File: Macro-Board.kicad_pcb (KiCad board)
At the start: 2 copper layers, 215.9 x 139.7 mm, 62 parts, among them J1 esp32row1, J2 esp32row1, K1 KEYSW, K10 KEYSW, K11 KEYSW, K12 KEYSW, K13 KEYSW, K14 KEYSW, K15 KEYSW, K16 KEYSW, K17 KEYSW, K18 KEYSW, K19 KEYSW, K2 KEYSW, K20 KEYSW, K21 KEYSW, K22 KEYSW, K23 KEYSW, K24 KEYSW, K25 KEYSW, K27 KEYSW, K28 KEYSW, K29 KEYSW, K3 KEYSW, K30 KEYSW, K4 KEYSW, K5 KEYSW, K6 KEYSW, K7 KEYSW, K8 KEYSW, K9 KEYSW, SW26 RotaryEncoder_Alps_EC11E-Swit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

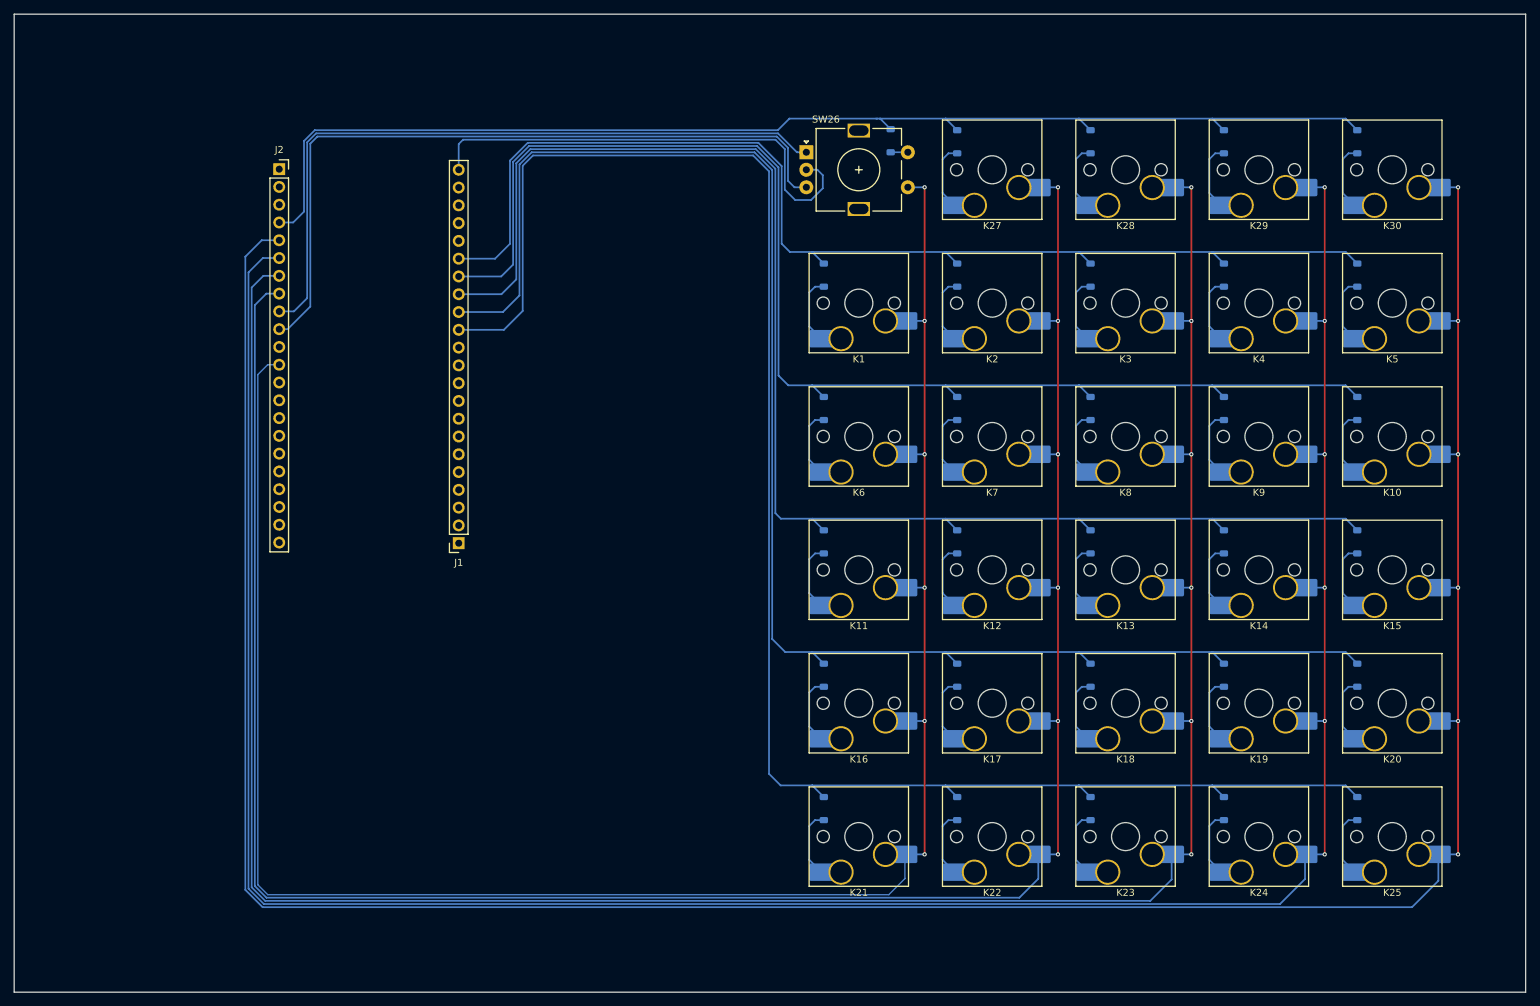
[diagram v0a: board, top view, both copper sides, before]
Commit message: Added PCB Edge + Updated Encoder Library
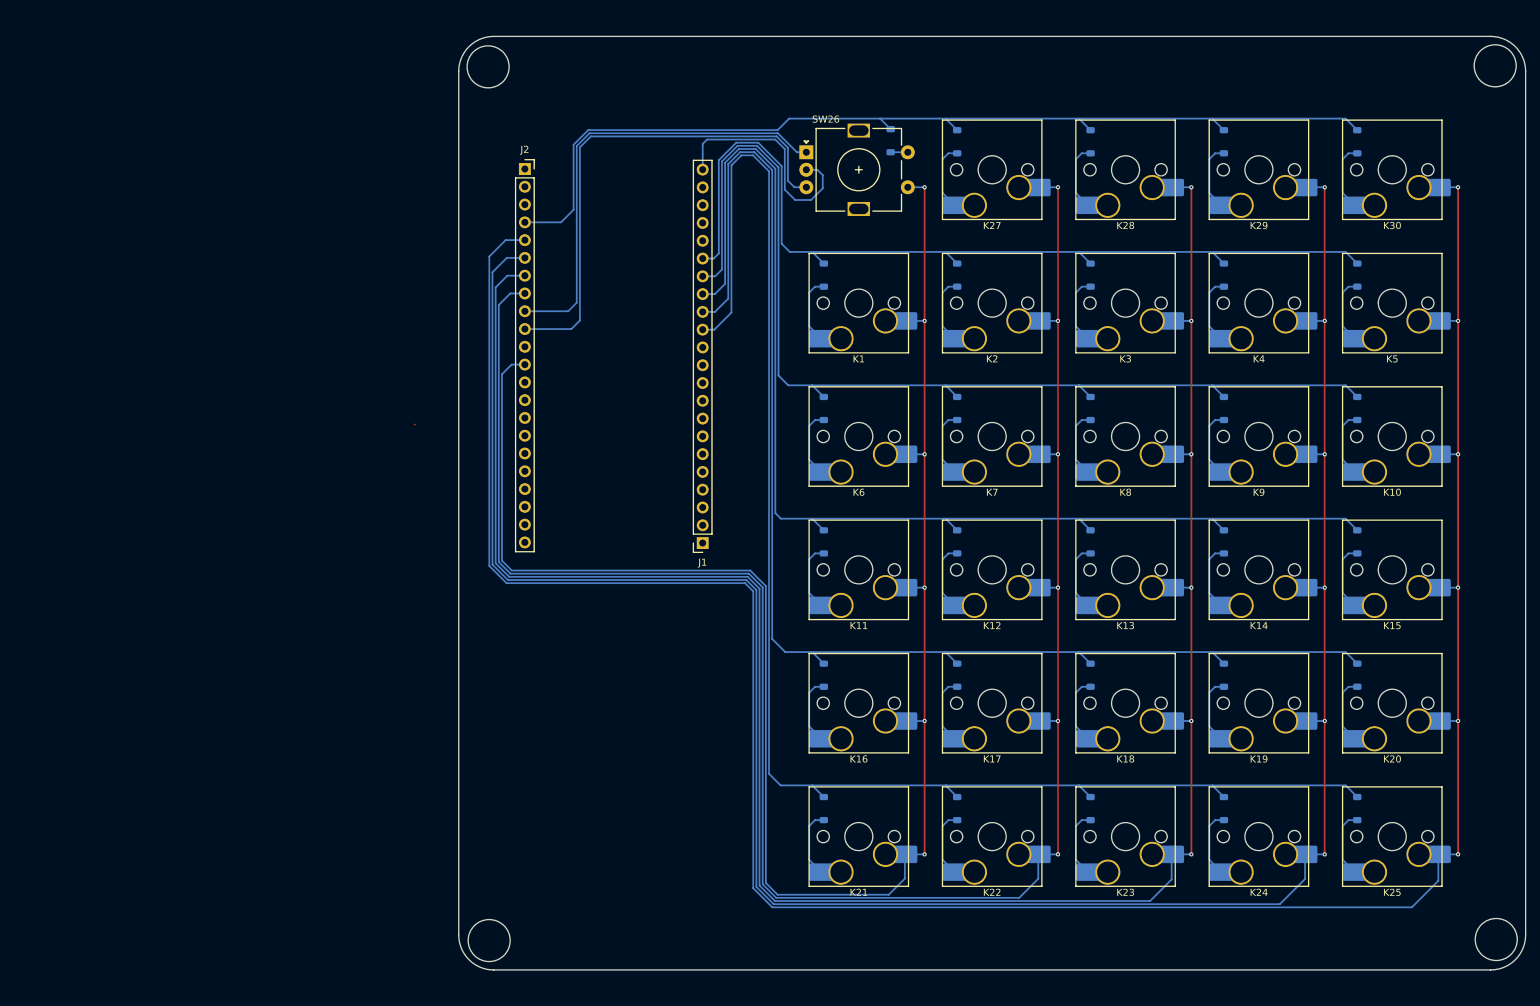
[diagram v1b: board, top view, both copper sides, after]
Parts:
- moved J2 35.1 mm to (-47.7, -19.2)
- moved J1 34.9 mm to (-22.3, 34.3)
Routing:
- net /GPIO08: track 285.7 -> 248.6 mm
- net /GPIO05: track 384.8 -> 347.7 mm
- net /GPIO06: track 361.9 -> 324.8 mm
- net /GPIO07: track 339.1 -> 302.0 mm
- net /GPIO15: track 316.1 -> 279.0 mm
- net /GPIO04: track 175.9 -> 140.6 mm
- net /GND4: track 68.1 -> 33.3 mm
- net /EncoderA: track 100.0 -> 65.2 mm
- net /GPIO38: track 248.6 -> 213.9 mm
- net /GPIO39: track 227.6 -> 193.1 mm
- net /GPIO40: track 207.4 -> 173.0 mm
- net /GPIO41: track 186.3 -> 151.9 mm
- net /GPIO42: track 165.2 -> 131.2 mm
- net /EncoderB: track 106.1 -> 72.1 mm
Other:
- board size 215.9 x 139.7 mm -> 152.4 x 133.3 mm

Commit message: idk
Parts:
- moved J1 70.5 mm to (-43.0, -33.1), turned to 0 degrees
- moved J2 49.7 mm to (-17.6, 20.3), turned to 180 degrees
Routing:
- net /EncoderB: track 72.1 -> 10.0 mm
- net /EncoderA: track 65.2 -> 5.19 mm
- net /GPIO05: track 347.7 -> 297.7 mm
- net /GPIO04: track 140.6 -> 93.3 mm
- net /GPIO06: track 324.8 -> 277.8 mm
- net /GPIO07: track 302.0 -> 258.0 mm
- net /GPIO15: track 279.0 -> 238.2 mm
- net /GPIO38: track 213.9 -> 180.8 mm
- net /GPIO39: track 193.1 -> 161.4 mm
- net /GPIO40: track 173.0 -> 142.7 mm
- net /GPIO08: track 248.6 -> 218.3 mm
- net /GPIO41: track 151.9 -> 123.1 mm
- net /GPIO42: track 131.2 -> 103.9 mm
- net /GND4: track 33.3 -> 19.0 mm
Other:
- outline, holes or cut-outs redrawn

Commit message: Idfk
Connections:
- D1 pad 1: /GPIO42 -> /GPIO16
- D10 pad 1: /GPIO41 -> /GPIO15
- D11 pad 1: /GPIO40 -> /GPIO07
- D12 pad 1: /GPIO40 -> /GPIO07
- D13 pad 1: /GPIO40 -> /GPIO07
- D14 pad 1: /GPIO40 -> /GPIO07
- D15 pad 1: /GPIO40 -> /GPIO07
- D16 pad 1: /GPIO39 -> /GPIO06
- D17 pad 1: /GPIO39 -> /GPIO06
- D18 pad 1: /GPIO39 -> /GPIO06
- D19 pad 1: /GPIO39 -> /GPIO06
- D2 pad 1: /GPIO42 -> /GPIO16
- D20 pad 1: /GPIO39 -> /GPIO06
- D21 pad 1: /GPIO38 -> /GPIO05
- D22 pad 1: /GPIO38 -> /GPIO05
- D23 pad 1: /GPIO38 -> /GPIO05
- D24 pad 1: /GPIO38 -> /GPIO05
- D25 pad 1: /GPIO38 -> /GPIO05
- D26 pad 1: /GPIO04 -> /GPIO17
- D27 pad 1: /GPIO04 -> /GPIO17
- D28 pad 1: /GPIO04 -> /GPIO17
- D29 pad 1: /GPIO04 -> /GPIO17
- D3 pad 1: /GPIO42 -> /GPIO16
- D30 pad 1: /GPIO04 -> /GPIO17
- D4 pad 1: /GPIO42 -> /GPIO16
- D5 pad 1: /GPIO42 -> /GPIO16
- D6 pad 1: /GPIO41 -> /GPIO15
- D7 pad 1: /GPIO41 -> /GPIO15
- D8 pad 1: /GPIO41 -> /GPIO15
- D9 pad 1: /GPIO41 -> /GPIO15
- J2 pad 10: /EncoderB -> /GPIO17
- J2 pad 11: /GPIO18 -> /EncoderA
- J2 pad 12: /GPIO08 -> /EncoderB
- J2 pad 9: /EncoderA -> /GPIO16
- K1 pad 1: /GPIO08 -> /GPIO01
- K10 pad 1: /GPIO05 -> /GPIO40
- K11 pad 1: /GPIO08 -> /GPIO01
- K12 pad 1: /GPIO15 -> /GPIO02
- K13 pad 1: /GPIO07 -> /GPIO42
- K14 pad 1: /GPIO06 -> /GPIO41
- K15 pad 1: /GPIO05 -> /GPIO40
- K16 pad 1: /GPIO08 -> /GPIO01
- K17 pad 1: /GPIO15 -> /GPIO02
- K18 pad 1: /GPIO07 -> /GPIO42
- K19 pad 1: /GPIO06 -> /GPIO41
- K2 pad 1: /GPIO15 -> /GPIO02
- K20 pad 1: /GPIO05 -> /GPIO40
- K21 pad 1: /GPIO08 -> /GPIO01
- K22 pad 1: /GPIO15 -> /GPIO02
- K23 pad 1: /GPIO07 -> /GPIO42
- K24 pad 1: /GPIO06 -> /GPIO41
- K25 pad 1: /GPIO05 -> /GPIO40
- K27 pad 1: /GPIO15 -> /GPIO02
- K28 pad 1: /GPIO07 -> /GPIO42
- K29 pad 1: /GPIO06 -> /GPIO41
- K3 pad 1: /GPIO07 -> /GPIO42
- K30 pad 1: /GPIO05 -> /GPIO40
- K4 pad 1: /GPIO06 -> /GPIO41
- K5 pad 1: /GPIO05 -> /GPIO40
- K6 pad 1: /GPIO08 -> /GPIO01
- K7 pad 1: /GPIO15 -> /GPIO02
- K8 pad 1: /GPIO07 -> /GPIO42
- K9 pad 1: /GPIO06 -> /GPIO41
- SW26 pad C: /GND4 -> /GND1
- SW26 pad S1: /GPIO08 -> /GPIO01
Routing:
- net /GPIO02: track 0.00 -> 259.7 mm, vias 0 -> 6
- net /GPIO01: track 0.00 -> 235.5 mm, vias 0 -> 6
- net /GPIO08: track 218.3 -> 0.00 mm, vias 6 -> 0
- net /GPIO40: track 142.7 -> 329.2 mm, vias 0 -> 6
- net /GPIO41: track 123.1 -> 305.9 mm, vias 0 -> 6
- net /GPIO38: track 180.8 -> 0.00 mm
- net /GPIO42: track 103.9 -> 282.9 mm, vias 0 -> 6
- net /GPIO39: track 161.4 -> 0.00 mm
- net /GPIO17: track 0.00 -> 144.8 mm
- net /GPIO05: track 297.7 -> 159.4 mm, vias 6 -> 0
- net /GPIO06: track 277.8 -> 141.6 mm, vias 6 -> 0
- net /GPIO15: track 238.2 -> 102.7 mm, vias 6 -> 0
- net /GPIO07: track 258.0 -> 123.8 mm, vias 6 -> 0
- net /GPIO16: track 0.00 -> 106.4 mm
- net /GPIO04: track 93.3 -> 0.00 mm
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
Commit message: cosmetic changes
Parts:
- J2: value esp32row1 -> esp32row2
- renumbered K1 to SW1, K10 to SW10, K11 to SW11, K12 to SW12, K13 to SW13, K14 to SW14, K15 to SW15, K16 to SW16, K17 to SW17, K18 to SW18, K19 to SW19, K2 to SW2, K20 to SW20, K21 to SW21, K22 to SW22, K23 to SW23, K24 to SW24, K25 to SW25, K27 to SW27, K28 to SW28, K29 to SW29, K3 to SW3, K30 to SW30, K4 to SW4, K5 to SW5, K6 to SW6, K7 to SW7, K8 to SW8, K9 to SW9
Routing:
- net /GPIO01: track 235.5 -> 237.3 mm
